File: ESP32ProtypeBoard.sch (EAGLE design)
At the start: 102 parts, among them IC1 SOIC-8, IC2 SI4431BDY, J10 POWER_JACKPTH_LOCK, Q2 MMBT3904, Q3 MMBT3904, U2 ESP-WROOM-32

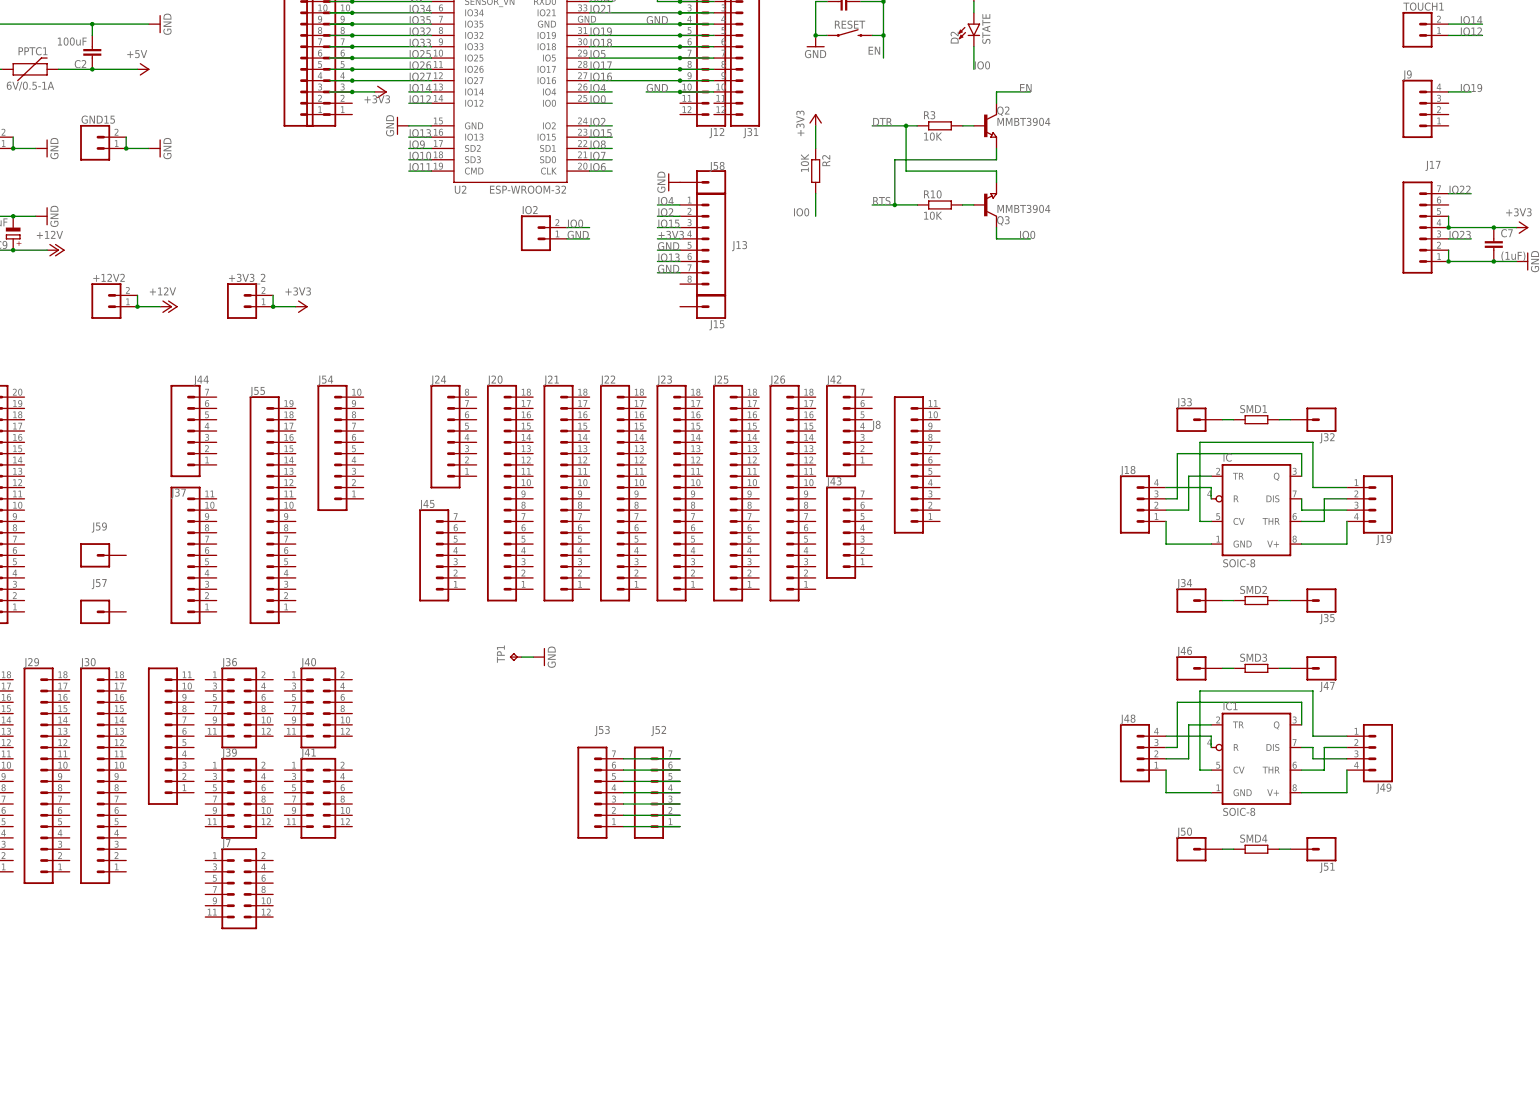
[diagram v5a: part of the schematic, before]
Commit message: Smarter space extra SMD, completed pinout
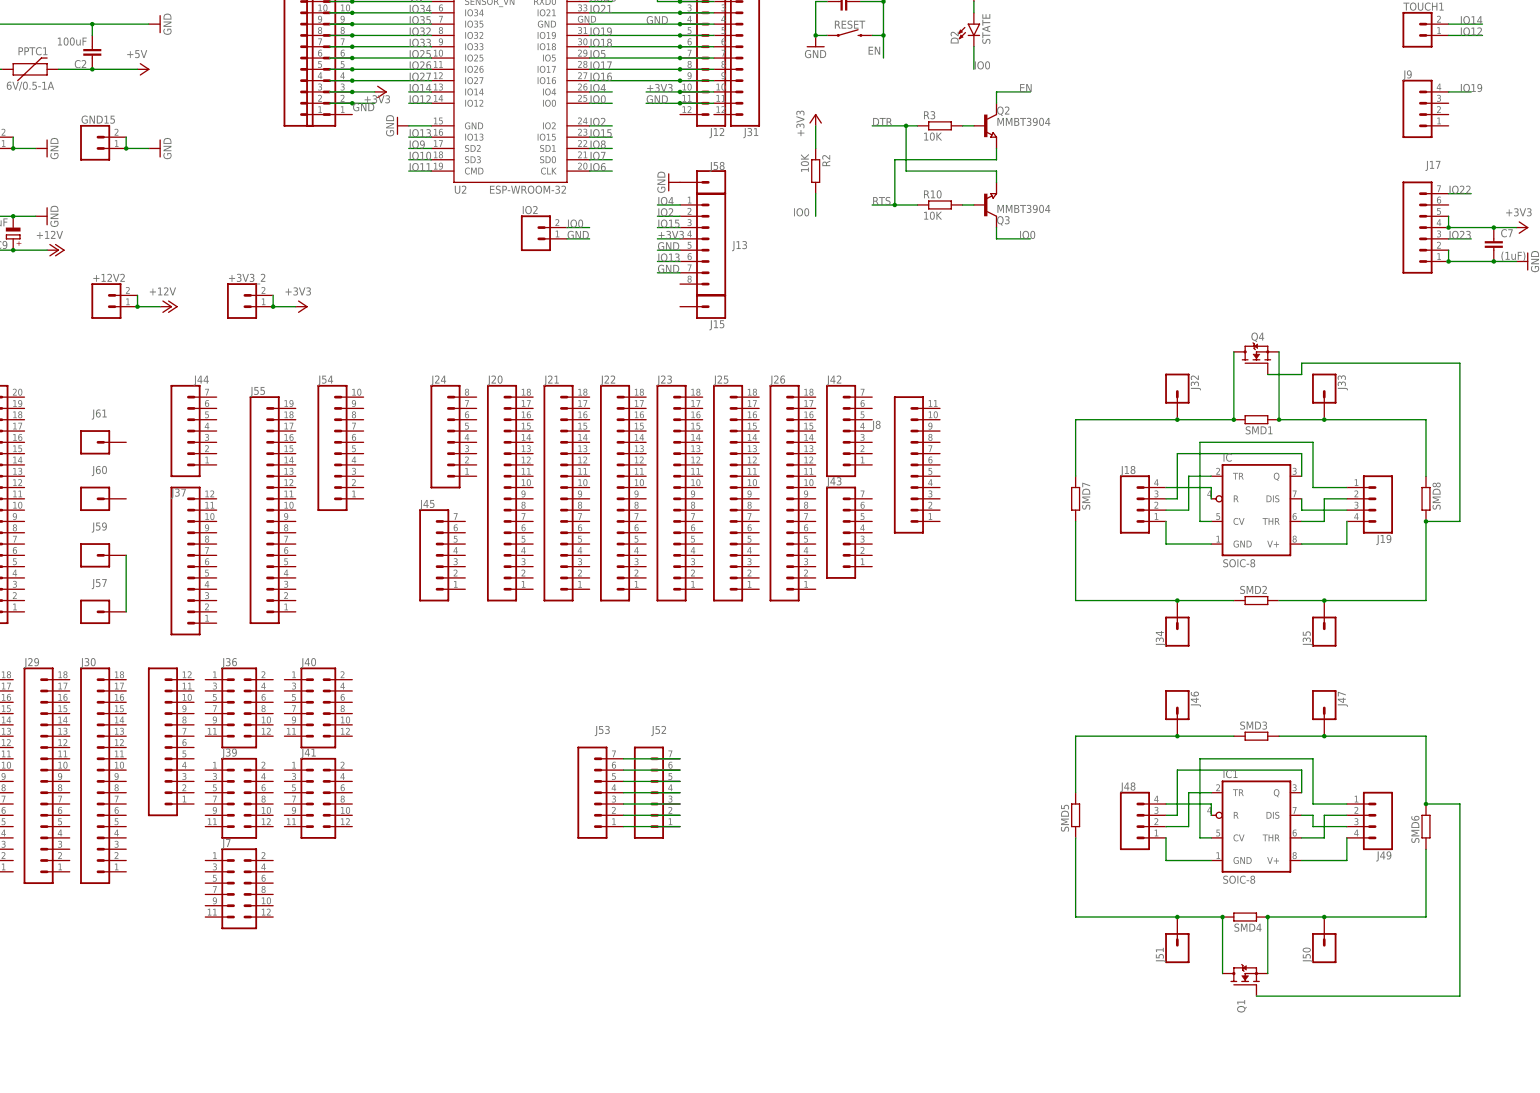
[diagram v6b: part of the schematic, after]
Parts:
- removed TP1: TPTP15SQ, testpad:TPTP15SQ
- added J60, J61: (no value), SparkFun-Connectors:CONN_01PTH_NO_SILK_KIT
- added Q1, Q4: BSS138, bss138_10:BSS138
- added SMD5, SMD6, SMD7, SMD8: (no value), eagle-ltspice:RR1206
- J37, J38: device SparkFun-Connectors:CONN_111X11_NO_SILK -> SparkFun-Connectors:CONN_12NO_SILK
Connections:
- removed net N$13: J33.1, SMD1.1
- removed net N$14: J32.1, SMD1.2
- new net N$51: J57.1, J59.1
- new net N$53: J51.1, Q1.D, SMD4.2, SMD5.1
- new net N$55: J47.1, Q1.G, SMD3.2, SMD6.2
- net +3V3: now also J12.10, J31.10
- net GND: now also J11.2, J12.11, J14.2, J31.11; no longer J12.10, J31.10, TP1.TP
- net N$15: now also SMD7.2
- net N$16: now also Q4.G, SMD8.2
- net N$17: now also SMD5.2
- net N$18: now also J32.1, Q4.D, SMD1.2, SMD7.1; no longer J47.1, SMD3.2
- net N$19: now also J33.1, Q4.S, SMD1.1, SMD8.1; no longer J50.1, SMD4.1
- net N$20: now also J50.1, Q1.S, SMD4.1, SMD6.1; no longer J51.1, SMD4.2
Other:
- moved on the sheet: IC1, J32, J33, J34, J35, J46, J47, J48, J49, J50, J51, SMD1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

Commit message: FINAL version
Fixed all silk, moved optional cap
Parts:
- removed Q4: BSS138, bss138_10:BSS138
- added Q5: (no value), semicon-smd-ipc:NPN-TRANSISTOR_SOT23
- Q1: value BSS138 -> (none); device bss138_10:BSS138 -> semicon-smd-ipc:NPN-TRANSISTOR_SOT23
- R1: value 150R -> 220R
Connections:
- net N$16: now also Q1.B; no longer Q4.G
- net N$18: now also Q1.C; no longer Q4.D
- net N$19: now also Q1.E; no longer Q4.S
- net N$20: now also Q5.E; no longer Q1.S
- net N$53: now also Q5.C; no longer Q1.D
- net N$55: now also Q5.B; no longer Q1.G
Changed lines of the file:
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@@
 <part name="P+10" library="supply1" library_urn="urn:adsk.eagle:library:371" deviceset="VCC" device=""/>
 <part name="D2" library="SparkFun-LED" deviceset="LED-GREEN" device="1206" value="STATE"/>
-<part name="R1" library="eagle-ltspice" library_urn="urn:adsk.eagle:library:217" deviceset="R" device="R1206" package3d_urn="urn:adsk.eagle:package:13301/1" value="150R"/>
+<part name="R1" library="eagle-ltspice" library_urn="urn:adsk.eagle:library:217" deviceset="R" device="R1206" package3d_urn="urn:adsk.eagle:package:13301/1" value="220R"/>
 <part name="J4" library="SparkFun-Connectors" library_urn="urn:adsk.eagle:library:513" deviceset="CONN_02" device="1X02_NO_SILK" package3d_urn="urn:adsk.eagle:package:38051/1"/>
 <part name="J5" library="SparkFun-Connectors" deviceset="CONN_16" device="1X16_NO_SILK"/>
@@
 <part name="J60" library="SparkFun-Connectors" library_urn="urn:adsk.eagle:library:513" deviceset="CONN_01" device="PTH_NO_SILK_KIT" package3d_urn="urn:adsk.eagle:package:38038/1"/>
 <part name="J61" library="SparkFun-Connectors" library_urn="urn:adsk.eagle:library:513" deviceset="CONN_01" device="PTH_NO_SILK_KIT" package3d_urn="urn:adsk.eagle:package:38038/1"/>
-<part name="Q1" library="bss138_10" deviceset="BSS138" device=""/>
 <part name="SMD5" library="eagle-ltspice" library_urn="urn:adsk.eagle:library:217" deviceset="R" device="R1206" package3d_urn="urn:adsk.eagle:package:13301/1"/>
 <part name="SMD6" library="eagle-ltspice" library_urn="urn:adsk.eagle:library:217" deviceset="R" device="R1206" package3d_urn="urn:adsk.eagle:package:13301/1"/>
-<part name="Q4" library="bss138_10" deviceset="BSS138" device=""/>
 <part name="SMD7" library="eagle-ltspice" library_urn="urn:adsk.eagle:library:217" deviceset="R" device="R1206" package3d_urn="urn:adsk.eagle:package:13301/1"/>
 <part name="SMD8" library="eagle-ltspice" library_urn="urn:adsk.eagle:library:217" deviceset="R" device="R1206" package3d_urn="urn:adsk.eagle:package:13301/1"/>
+<part name="Q5" library="semicon-smd-ipc" library_urn="urn:adsk.eagle:library:353" deviceset="NPN-TRANSISTOR_" device="SOT23" package3d_urn="urn:adsk.eagle:package:28738/2"/>
+<part name="Q1" library="semicon-smd-ipc" library_urn="urn:adsk.eagle:library:353" deviceset="NPN-TRANSISTOR_" device="SOT23" package3d_urn="urn:adsk.eagle:package:28738/2"/>
 </parts>
 <sheets>
@@
 <attribute name="NAME" x="104.14" y="-24.892" size="1.778" layer="95" font="vector"/>
 </instance>
-<instance part="Q1" gate="G$1" x="363.22" y="-152.4" smashed="yes" rot="R90">
-<attribute name="NAME" x="363.22" y="-158.75" size="1.778" layer="95" rot="R90"/>
-</instance>
 <instance part="SMD5" gate="G$1" x="325.12" y="-114.3" smashed="yes" rot="R90">
 <attribute name="NAME" x="323.6214" y="-118.11" size="1.778" layer="95" rot="R90"/>
@@
 <attribute name="VALUE" x="407.162" y="-120.65" size="1.778" layer="96" rot="R90"/>
 </instance>
-<instance part="Q4" gate="G$1" x="365.76" y="-12.7" smashed="yes" rot="R90">
-<attribute name="NAME" x="364.49" y="-7.62" size="1.778" layer="95"/>
-</instance>
 <instance part="SMD7" gate="G$1" x="325.12" y="-43.18" smashed="yes" rot="R270">
 <attribute name="NAME" x="326.6186" y="-39.37" size="1.778" layer="95" rot="R270"/>
@@
 <attribute name="NAME" x="405.3586" y="-39.37" size="1.778" layer="95" rot="R270"/>
 <attribute name="VALUE" x="400.558" y="-39.37" size="1.778" layer="96" rot="R270"/>
+</instance>
+<instance part="Q5" gate="G$1" x="363.22" y="-152.4" smashed="yes" rot="R90">
+<attribute name="NAME" x="360.68" y="-149.86" size="1.778" layer="95" rot="R90"/>
+<attribute name="VALUE" x="363.22" y="-149.86" size="1.778" layer="96" rot="R90"/>
+</instance>
+<instance part="Q1" gate="G$1" x="365.76" y="-15.24" smashed="yes" rot="MR270">
+<attribute name="NAME" x="363.22" y="-17.78" size="1.778" layer="95" rot="MR270"/>
+<attribute name="VALUE" x="365.76" y="-17.78" size="1.778" layer="96" rot="MR270"/>
 </instance>
 </instances>
@@
 <wire x1="403.86" y1="-66.04" x2="381" y2="-66.04" width="0.1524" layer="91"/>
 <junction x="381" y="-66.04"/>
-<pinref part="Q4" gate="G$1" pin="G"/>
-<wire x1="368.3" y1="-15.24" x2="375.92" y2="-15.24" width="0.1524" layer="91"/>
-<wire x1="375.92" y1="-15.24" x2="375.92" y2="-12.7" width="0.1524" layer="91"/>
-<wire x1="375.92" y1="-12.7" x2="411.48" y2="-12.7" width="0.1524" layer="91"/>
+<wire x1="365.76" y1="-12.7" x2="411.48" y2="-12.7" width="0.1524" layer="91"/>
 <wire x1="411.48" y1="-12.7" x2="411.48" y2="-48.26" width="0.1524" layer="91"/>
 <wire x1="411.48" y1="-48.26" x2="403.86" y2="-48.26" width="0.1524" layer="91"/>
 <junction x="403.86" y="-48.26"/>
+<pinref part="Q1" gate="G$1" pin="B"/>
 </segment>
 </net>
@@
 <wire x1="403.86" y1="-137.16" x2="381" y2="-137.16" width="0.1524" layer="91"/>
 <junction x="381" y="-137.16"/>
-<pinref part="Q1" gate="G$1" pin="S"/>
+<junction x="368.3" y="-137.16"/>
 <wire x1="368.3" y1="-149.86" x2="368.3" y2="-137.16" width="0.1524" layer="91"/>
-<junction x="368.3" y="-137.16"/>
+<pinref part="Q5" gate="G$1" pin="E"/>
 </segment>
 </net>
@@
 <wire x1="347.98" y1="-137.16" x2="325.12" y2="-137.16" width="0.1524" layer="91"/>
 <junction x="347.98" y="-137.16"/>
-<pinref part="Q1" gate="G$1" pin="D"/>
 <wire x1="358.14" y1="-149.86" x2="358.14" y2="-137.16" width="0.1524" layer="91"/>
 <junction x="358.14" y="-137.16"/>
+<pinref part="Q5" gate="G$1" pin="C"/>
 </segment>
 </net>
@@
 <wire x1="381" y1="-96.52" x2="403.86" y2="-96.52" width="0.1524" layer="91"/>
 <junction x="381" y="-96.52"/>
-<pinref part="Q1" gate="G$1" pin="G"/>
-<wire x1="365.76" y1="-154.94" x2="411.48" y2="-154.94" width="0.1524" layer="91"/>
 <wire x1="411.48" y1="-154.94" x2="411.48" y2="-111.76" width="0.1524" layer="91"/>
 <wire x1="411.48" y1="-111.76" x2="403.86" y2="-111.76" width="0.1524" layer="91"/>
 <junction x="403.86" y="-111.76"/>
+<pinref part="Q5" gate="G$1" pin="B"/>
+<wire x1="363.22" y1="-154.94" x2="411.48" y2="-154.94" width="0.1524" layer="91"/>
 </segment>
 </net>
@@
 <wire x1="347.98" y1="-25.4" x2="325.12" y2="-25.4" width="0.1524" layer="91"/>
 <junction x="347.98" y="-25.4"/>
-<pinref part="Q4" gate="G$1" pin="D"/>
-<wire x1="360.68" y1="-10.16" x2="360.68" y2="-25.4" width="0.1524" layer="91"/>
+<wire x1="360.68" y1="-17.78" x2="360.68" y2="-25.4" width="0.1524" layer="91"/>
 <junction x="360.68" y="-25.4"/>
+<pinref part="Q1" gate="G$1" pin="C"/>
 </segment>
 </net>
@@
 <wire x1="381" y1="-25.4" x2="403.86" y2="-25.4" width="0.1524" layer="91"/>
 <junction x="381" y="-25.4"/>
-<pinref part="Q4" gate="G$1" pin="S"/>
-<wire x1="370.84" y1="-10.16" x2="370.84" y2="-25.4" width="0.1524" layer="91"/>
+<wire x1="370.84" y1="-17.78" x2="370.84" y2="-25.4" width="0.1524" layer="91"/>
 <junction x="370.84" y="-25.4"/>
-</segment>
-</net>
+<pinref part="Q1" gate="G$1" pin="E"/>
+</segment>
+</net>

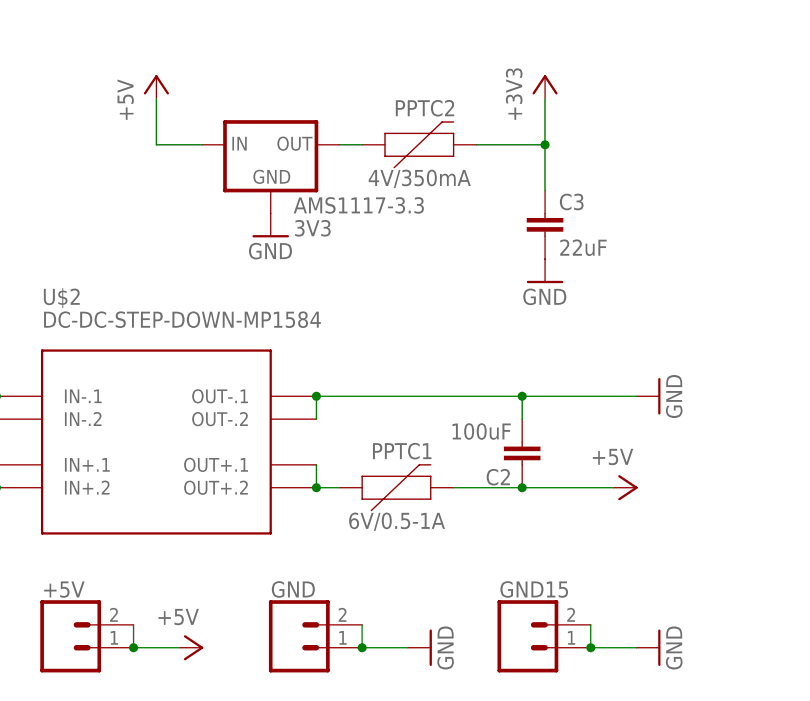
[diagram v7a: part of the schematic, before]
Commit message: Slight route adjustments
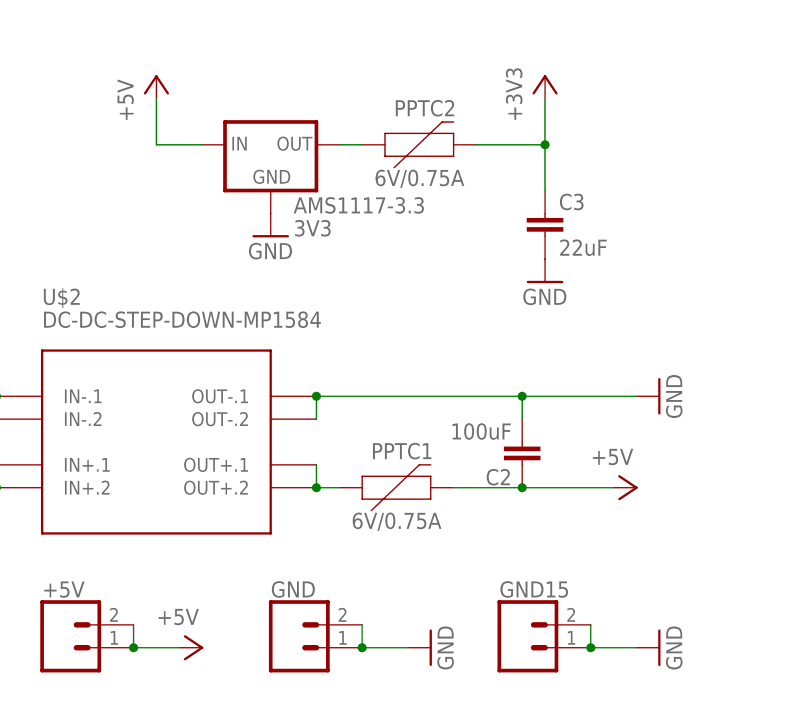
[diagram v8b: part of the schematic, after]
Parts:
- PPTC1: value 6V/0.5-1A -> 6V/0.75A
- PPTC2: value 4V/350mA -> 6V/0.75A
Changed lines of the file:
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@@
 <?xml version="1.0" encoding="utf-8"?>
 <!DOCTYPE eagle SYSTEM "eagle.dtd">
-<eagle version="9.2.2">
+<eagle version="9.3.0">
 <drawing>
 <settings>
@@
 <part name="+3V2" library="supply1" library_urn="urn:adsk.eagle:library:371" deviceset="+3V3" device=""/>
 <part name="P+11" library="supply1" library_urn="urn:adsk.eagle:library:371" deviceset="VCC" device=""/>
-<part name="PPTC1" library="SparkFun-Fuses" deviceset="PPTC" device="_THREE-QUARTER-AMP" value="6V/0.5-1A"/>
-<part name="PPTC2" library="SparkFun-Fuses" deviceset="PPTC" device="_THREE-QUARTER-AMP" value="4V/350mA"/>
+<part name="PPTC1" library="SparkFun-Fuses" library_urn="urn:adsk.eagle:library:517" deviceset="PPTC" device="_THREE-QUARTER-AMP" package3d_urn="urn:adsk.eagle:package:38575/1" value="6V/0.75A"/>
+<part name="PPTC2" library="SparkFun-Fuses" library_urn="urn:adsk.eagle:library:517" deviceset="PPTC" device="_THREE-QUARTER-AMP" package3d_urn="urn:adsk.eagle:package:38575/1" value="6V/0.75A"/>
 <part name="+3V10" library="supply1" library_urn="urn:adsk.eagle:library:371" deviceset="+3V3" device=""/>
 <part name="GND4" library="supply1" library_urn="urn:adsk.eagle:library:371" deviceset="GND" device=""/>
@@
 <attribute name="VALUE" x="22.86" y="15.24" size="1.778" layer="96" rot="R180"/>
 </instance>
-<instance part="PPTC1" gate="F1" x="88.9" y="53.34" smashed="yes">
+<instance part="PPTC1" gate="G$1" x="88.9" y="53.34" smashed="yes">
 <attribute name="NAME" x="90.805" y="56.515" size="1.778" layer="95" font="vector" align="bottom-center"/>
 <attribute name="VALUE" x="90.17" y="50.546" size="1.778" layer="96" font="vector" align="top-center"/>
 </instance>
-<instance part="PPTC2" gate="F1" x="91.44" y="91.44" smashed="yes">
+<instance part="PPTC2" gate="G$1" x="91.44" y="91.44" smashed="yes">
 <attribute name="NAME" x="93.345" y="94.615" size="1.778" layer="95" font="vector" align="bottom-center"/>
 <attribute name="VALUE" x="92.71" y="88.646" size="1.778" layer="96" font="vector" align="top-center"/>
@@
 <pinref part="+3V4" gate="G$1" pin="+3V3"/>
 <wire x1="106.68" y1="91.44" x2="106.68" y2="96.52" width="0.1524" layer="91"/>
-<pinref part="PPTC2" gate="F1" pin="2"/>
+<pinref part="PPTC2" gate="G$1" pin="2"/>
 <wire x1="99.06" y1="91.44" x2="106.68" y2="91.44" width="0.1524" layer="91"/>
 <pinref part="C3" gate="G$1" pin="1"/>
@@
 <pinref part="P+1" gate="1" pin="+5V"/>
 <wire x1="96.52" y1="53.34" x2="104.14" y2="53.34" width="0.1524" layer="91"/>
-<pinref part="PPTC1" gate="F1" pin="2"/>
+<pinref part="PPTC1" gate="G$1" pin="2"/>
 </segment>
 <segment>
@@
 <net name="5VOUT" class="0">
 <segment>
-<pinref part="PPTC1" gate="F1" pin="1"/>
+<pinref part="PPTC1" gate="G$1" pin="1"/>
 <pinref part="U$2" gate="G$1" pin="OUT+.2"/>
 <pinref part="U$2" gate="G$1" pin="OUT+.1"/>
@@
 <pinref part="AMS1117-3.3" gate="G$1" pin="OUT"/>
 <wire x1="83.82" y1="91.44" x2="86.36" y2="91.44" width="0.1524" layer="91"/>
-<pinref part="PPTC2" gate="F1" pin="1"/>
-</segment>
-</net>
+<pinref part="PPTC2" gate="G$1" pin="1"/>
+</segment>
+</net>
